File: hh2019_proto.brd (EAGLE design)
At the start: 263.1 x 150 mm, 150 parts, among them IC1 CP210X_USB_UART, IC2 AP2114H, IC4 TP4056, J1 PJ-313D, Q1 MMBT2222A, Q3 MMBT2222A, Q4 MMBT2222A, Q5 SI1304 BDL, U1 MPR121QR2, U2 ESP32-WROVER-I, U3 PCM5102A, X4 JST-PH3

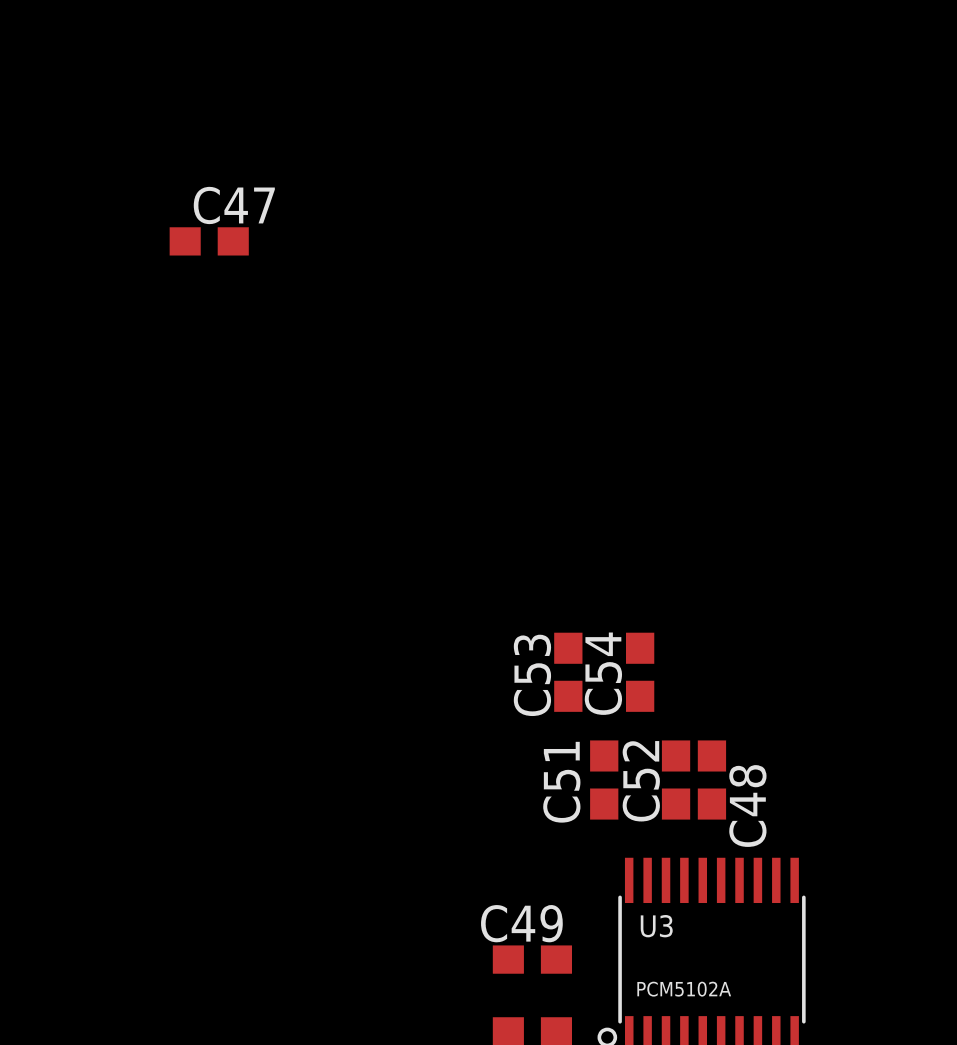
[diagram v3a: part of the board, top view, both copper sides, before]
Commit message: Removed some bypass caps from DAC
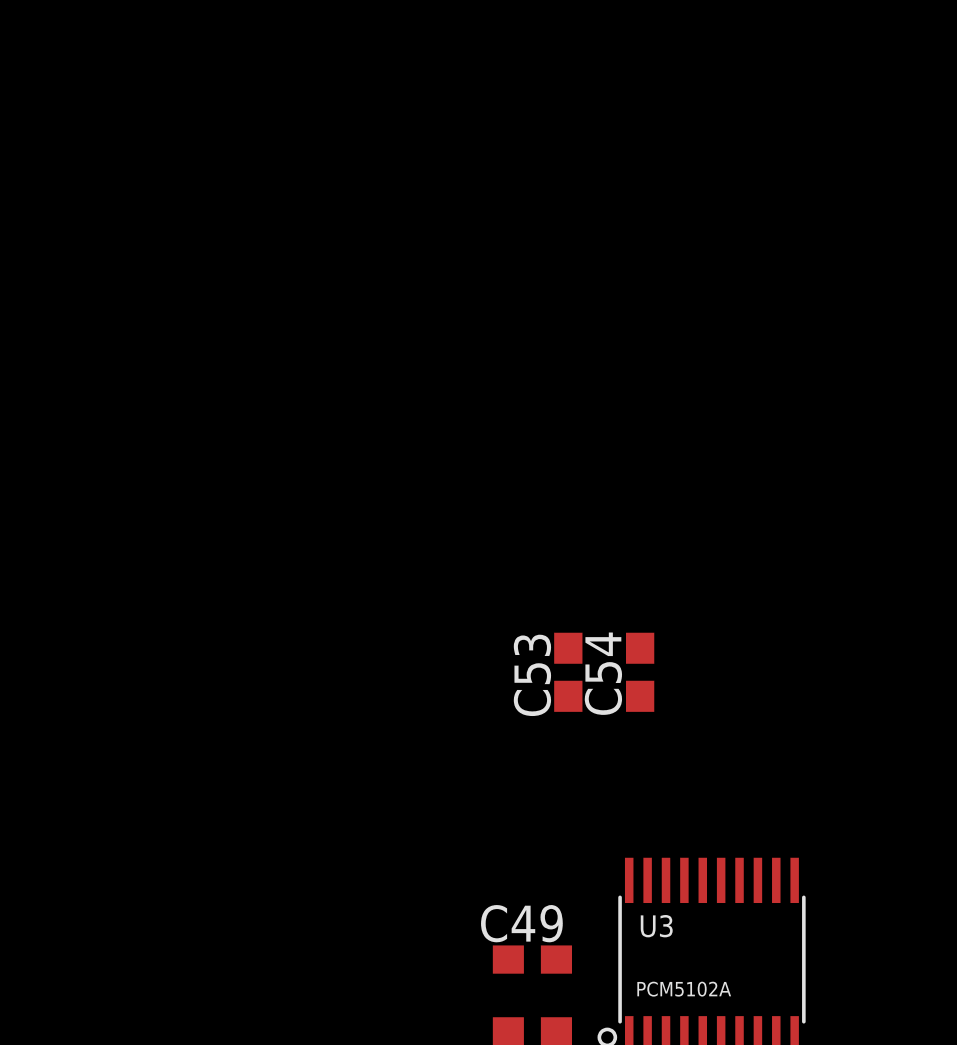
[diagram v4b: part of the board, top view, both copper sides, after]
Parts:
- removed C47, C51: 100n, rcl:C0603
- removed C48, C52: 1u, rcl:C0603
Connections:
- net 3V3: no longer C47.2, C48.2, C51.2, C52.2
- net GND: no longer C47.1, C48.1, C51.1, C52.1
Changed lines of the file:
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@@
 <attribute name="VALUE" x="323.215" y="74.295" size="1.27" layer="27"/>
-</element>
-<element name="C47" library="rcl" library_urn="urn:adsk.eagle:library:334" package="C0603" package3d_urn="urn:adsk.eagle:package:23616/2" value="100n" x="285.75" y="67.31" smashed="yes">
-<attribute name="NAME" x="285.115" y="67.945" size="1.27" layer="25"/>
-<attribute name="SPICEPREFIX" value="C" x="285.75" y="67.31" size="1.778" layer="27" display="off"/>
-<attribute name="VALUE" x="285.115" y="65.405" size="1.27" layer="27"/>
-</element>
-<element name="C48" library="rcl" library_urn="urn:adsk.eagle:library:334" package="C0603" package3d_urn="urn:adsk.eagle:package:23616/2" value="1u" x="303.53" y="48.26" smashed="yes" rot="R270">
-<attribute name="NAME" x="304.165" y="48.895" size="1.27" layer="25" rot="R270"/>
-<attribute name="SPICEPREFIX" value="C" x="303.53" y="48.26" size="1.778" layer="27" rot="R270" display="off"/>
-<attribute name="VALUE" x="301.625" y="48.895" size="1.27" layer="27" rot="R270"/>
 </element>
 <element name="C49" library="rcl" library_urn="urn:adsk.eagle:library:334" package="C0603" package3d_urn="urn:adsk.eagle:package:23616/2" value="1u" x="297.18" y="41.91" smashed="yes">
@@
 <attribute name="SPICEPREFIX" value="C" x="297.18" y="39.37" size="1.778" layer="27" rot="R180" display="off"/>
 <attribute name="VALUE" x="297.815" y="41.275" size="1.27" layer="27" rot="R180"/>
-</element>
-<element name="C51" library="rcl" library_urn="urn:adsk.eagle:library:334" package="C0603" package3d_urn="urn:adsk.eagle:package:23616/2" value="100n" x="299.72" y="48.26" smashed="yes" rot="R270">
-<attribute name="NAME" x="298.855" y="46.665" size="1.27" layer="25" rot="R90"/>
-<attribute name="SPICEPREFIX" value="C" x="299.72" y="48.26" size="1.778" layer="27" rot="R270" display="off"/>
-<attribute name="VALUE" x="297.815" y="48.895" size="1.27" layer="27" rot="R270"/>
-</element>
-<element name="C52" library="rcl" library_urn="urn:adsk.eagle:library:334" package="C0603" package3d_urn="urn:adsk.eagle:package:23616/2" value="1u" x="302.26" y="48.26" smashed="yes" rot="R270">
-<attribute name="NAME" x="300.395" y="49.795" size="1.27" layer="25" rot="R270"/>
-<attribute name="SPICEPREFIX" value="C" x="302.26" y="48.26" size="1.778" layer="27" rot="R270" display="off"/>
-<attribute name="VALUE" x="300.355" y="48.895" size="1.27" layer="27" rot="R270"/>
 </element>
 <element name="C53" library="rcl" library_urn="urn:adsk.eagle:library:334" package="C0603" package3d_urn="urn:adsk.eagle:package:23616/2" value="1u" x="298.45" y="52.07" smashed="yes" rot="R90">
@@
 <contactref element="U3" pad="P$3"/>
 <contactref element="C50" pad="2"/>
-<contactref element="C51" pad="1"/>
-<contactref element="C52" pad="1"/>
 <contactref element="U3" pad="P$19"/>
-<contactref element="C47" pad="1"/>
-<contactref element="C48" pad="1"/>
 <contactref element="C53" pad="2"/>
 <contactref element="C54" pad="2"/>
@@
 <wire x1="300.99" y1="52.92" x2="314.11" y2="76.2" width="0" layer="19" extent="1-1"/>
 <wire x1="298.45" y1="52.92" x2="300.99" y2="52.92" width="0" layer="19" extent="1-1"/>
-<wire x1="302.26" y1="49.11" x2="300.99" y2="52.92" width="0" layer="19" extent="1-1"/>
-<wire x1="303.53" y1="49.11" x2="302.26" y2="49.11" width="0" layer="19" extent="1-1"/>
-<wire x1="299.72" y1="49.11" x2="302.26" y2="49.11" width="0" layer="19" extent="1-1"/>
-<wire x1="303.205" y1="44.71" x2="303.53" y2="49.11" width="0" layer="19" extent="1-1"/>
-<wire x1="301.255" y1="44.71" x2="303.205" y2="44.71" width="0" layer="19" extent="1-1"/>
+<wire x1="301.255" y1="44.71" x2="300.99" y2="52.92" width="0" layer="19" extent="1-1"/>
+<wire x1="303.205" y1="44.71" x2="301.255" y2="44.71" width="0" layer="19" extent="1-1"/>
 <wire x1="306.455" y1="44.71" x2="303.205" y2="44.71" width="0" layer="19" extent="1-1"/>
 <wire x1="305.805" y1="39.11" x2="306.455" y2="44.71" width="0" layer="19" extent="1-1"/>
@@
 <wire x1="306.78" y1="29.21" x2="305.805" y2="39.11" width="0" layer="19" extent="1-1"/>
 <wire x1="300.28" y1="29.21" x2="306.78" y2="29.21" width="0" layer="19" extent="1-1"/>
-<wire x1="284.9" y1="67.31" x2="298.45" y2="52.92" width="0" layer="19" extent="1-1"/>
 <wire x1="110.49" y1="93.13" x2="200.66" y2="67.31" width="0" layer="19" extent="1-1"/>
 <wire x1="109.64" y1="93.98" x2="110.49" y2="93.13" width="0" layer="19" extent="1-1"/>
@@
 <contactref element="C40" pad="2"/>
 <contactref element="U3" pad="P$20"/>
-<contactref element="C47" pad="2"/>
-<contactref element="C48" pad="2"/>
 <contactref element="U3" pad="P$1"/>
-<contactref element="C51" pad="2"/>
-<contactref element="C52" pad="2"/>
 <wire x1="45.3" y1="173.99" x2="65.236971875" y2="166.680525" width="0" layer="19" extent="1-1"/>
 <wire x1="18.73" y1="148.59" x2="45.3" y2="173.99" width="0" layer="19" extent="1-1"/>
@@
 <wire x1="315.81" y1="76.2" x2="304.2" y2="104.93" width="0" layer="19" extent="1-1"/>
 <wire x1="324.7" y1="76.2" x2="315.81" y2="76.2" width="0" layer="19" extent="1-1"/>
-<wire x1="286.6" y1="67.31" x2="315.81" y2="76.2" width="0" layer="19" extent="1-1"/>
-<wire x1="299.72" y1="47.41" x2="286.6" y2="67.31" width="0" layer="19" extent="1-1"/>
-<wire x1="302.26" y1="47.41" x2="299.72" y2="47.41" width="0" layer="19" extent="1-1"/>
-<wire x1="303.53" y1="47.41" x2="302.26" y2="47.41" width="0" layer="19" extent="1-1"/>
-<wire x1="300.603" y1="44.71" x2="299.72" y2="47.41" width="0" layer="19" extent="1-1"/>
+<wire x1="300.603" y1="44.71" x2="315.81" y2="76.2" width="0" layer="19" extent="1-1"/>
 <wire x1="300.605" y1="39.11" x2="300.603" y2="44.71" width="0" layer="19" extent="1-1"/>
 <wire x1="305.155" y1="39.11" x2="300.605" y2="39.11" width="0" layer="19" extent="1-1"/>

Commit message: Prepping layout
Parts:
- moved U1 223.7 mm to (-121.9, 41.9)
- moved S2 221.9 mm to (285.8, 78.7)
- moved S1 210.4 mm to (275.6, 78.7)
- moved C1 78.7 mm to (125.7, 265.4)
- moved D105 78.7 mm to (121.9, 265.4)
- moved USB1 66.5 mm to (82.5, 174.0)
- moved C4 58.4 mm to (115.6, 265.4)
- moved D104 58.4 mm to (111.8, 265.4)
- moved C23 46.4 mm to (118.1, 214.6), turned to 270 degrees
- moved D103 44.5 mm to (101.6, 265.4)
- moved C24 43.6 mm to (115.6, 214.6), turned to 90 degrees
- moved C5 41.9 mm to (105.4, 265.4)
- moved SJ3 32.0 mm to (108.0, 199.4), turned to 0 degrees
- moved D102 29.2 mm to (91.4, 265.4)
- moved R35 28.0 mm to (108.0, 201.9), turned to 180 degrees
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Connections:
- net N$12 renamed CE
- net N$7 renamed PROG

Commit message: Added net names for touch controller pins (will remap touch buttons for easy routing later)
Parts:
- moved R36 2.84 mm to (94.0, 214.6)
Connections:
- net N$1 renamed ELE1
- net N$24 renamed ELE2
- net N$25 renamed ELE3
- net N$44 renamed ELE4
- net N$46 renamed ELE7
- net N$47 renamed ELE6
- net N$48 renamed ELE5
- net N$6 renamed ELE0
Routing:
- added copper zone on layer 1, net 3V3
- added copper zone on layer 16, net GND

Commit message: Collected components in groups in board design
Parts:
- moved R22 58.9 mm to (110.5, 161.3)
- moved R14 45.1 mm to (115.6, 179.1), turned to 90 degrees
- moved Q4 44.2 mm to (100.3, 163.8), turned to 90 degrees
- moved R3 37.7 mm to (83.8, 166.4), turned to 270 degrees
- moved R24 36.7 mm to (120.7, 160.0), turned to 270 degrees
- moved R23 35.4 mm to (116.8, 160.0), turned to 270 degrees
- moved R15 33.7 mm to (102.9, 161.3)
- moved X1 33.2 mm to (337.8, 110.5), turned to 180 degrees
- moved C44 32.5 mm to (43.2, 165.1), turned to 270 degrees
- moved C43 32.5 mm to (45.7, 165.1), turned to 270 degrees
- moved Q3 32.2 mm to (110.5, 166.4)
- moved R18 32.2 mm to (102.9, 166.4)
- moved C29 30.9 mm to (81.3, 104.1), turned to 270 degrees
- moved R16 30.3 mm to (113.0, 160.0), turned to 90 degrees
- moved Q5 30.2 mm to (342.9, 100.3), turned to 180 degrees
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
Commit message: Reassigned touch controller pins for easier layouting, got proper main component placement on board
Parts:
- moved X1 460.6 mm to (-122.2, 134.6)
- moved J1 424.2 mm to (-106.7, 137.2), turned to 90 degrees
- moved U2 413.0 mm to (-132.1, 116.8), turned to 90 degrees
- moved U3 411.8 mm to (-96.5, 139.7), turned to 270 degrees
- moved C54 409.9 mm to (-104.1, 114.3), turned to 0 degrees
- moved C53 409.1 mm to (-104.1, 111.8), turned to 0 degrees
- moved C50 407.1 mm to (-100.3, 127.0), turned to 0 degrees
- moved C49 406.0 mm to (-100.3, 124.5), turned to 180 degrees
- moved S2 402.8 mm to (-116.8, 67.3)
- moved S1 402.8 mm to (-127.0, 67.3)
- moved C1 321.4 mm to (-153.7, 106.7), turned to 180 degrees
- moved D105 320.0 mm to (-153.7, 102.9), turned to 0 degrees
- moved C4 317.8 mm to (-153.7, 96.5), turned to 180 degrees
- moved D104 316.7 mm to (-153.7, 92.7), turned to 0 degrees
- moved C5 314.9 mm to (-153.7, 86.4), turned to 180 degrees
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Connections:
- net ELE0: now also TOUCH_START.P$1; no longer TOUCH_A.P$1
- net ELE1: now also TOUCH_SELECT.P$1; no longer TOUCH_B.P$1
- net ELE2: now also TOUCH_B.P$1; no longer TOUCH_START.P$1
- net ELE3: now also TOUCH_SEL.R; no longer TOUCH_SELECT.P$1
- net ELE4: now also TOUCH_SEL.UP; no longer TOUCH_SEL.D
- net ELE5: now also TOUCH_SEL.L; no longer TOUCH_SEL.R
- net ELE6: now also TOUCH_SEL.D; no longer TOUCH_SEL.UP
- net ELE7: now also TOUCH_A.P$1; no longer TOUCH_SEL.L
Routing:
- net I2C_SDA: track 0.00 -> 69.4 mm, vias 0 -> 2
- net I2C_SCL: track 0.00 -> 68.7 mm, vias 0 -> 2
- net I2C_INT: track 0.00 -> 68.4 mm
- net ELE6: track 0.00 -> 65.8 mm, vias 0 -> 1
- net ESP32_!RESET: track 0.00 -> 44.4 mm
- net WS2812_POWER_EN: track 0.00 -> 42.2 mm, vias 0 -> 2
- net ELE3: track 0.00 -> 35.6 mm, vias 0 -> 1
- net 3V3: track 0.00 -> 30.9 mm, vias 0 -> 2
- net ELE5: track 0.00 -> 30.9 mm, vias 0 -> 1
- net GND: track 0.00 -> 23.2 mm, vias 0 -> 7
- net LCD_!RESET: track 0.00 -> 21.6 mm, vias 0 -> 1
- net ELE0: track 0.00 -> 20.4 mm, vias 0 -> 1
- net LCD_BUSY: track 0.00 -> 18.9 mm, vias 0 -> 1
- net ELE2: track 0.00 -> 15.0 mm, vias 0 -> 1
- net LCD_D/!S: track 0.00 -> 14.9 mm
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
